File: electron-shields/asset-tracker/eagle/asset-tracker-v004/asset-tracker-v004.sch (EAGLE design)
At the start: 23 parts, among them J1 1X2-3.5MM, T1 DMG3415, U1 PAM-7Q-GPS-TH, U3 LIS3DHTR, X1 ELECTRON

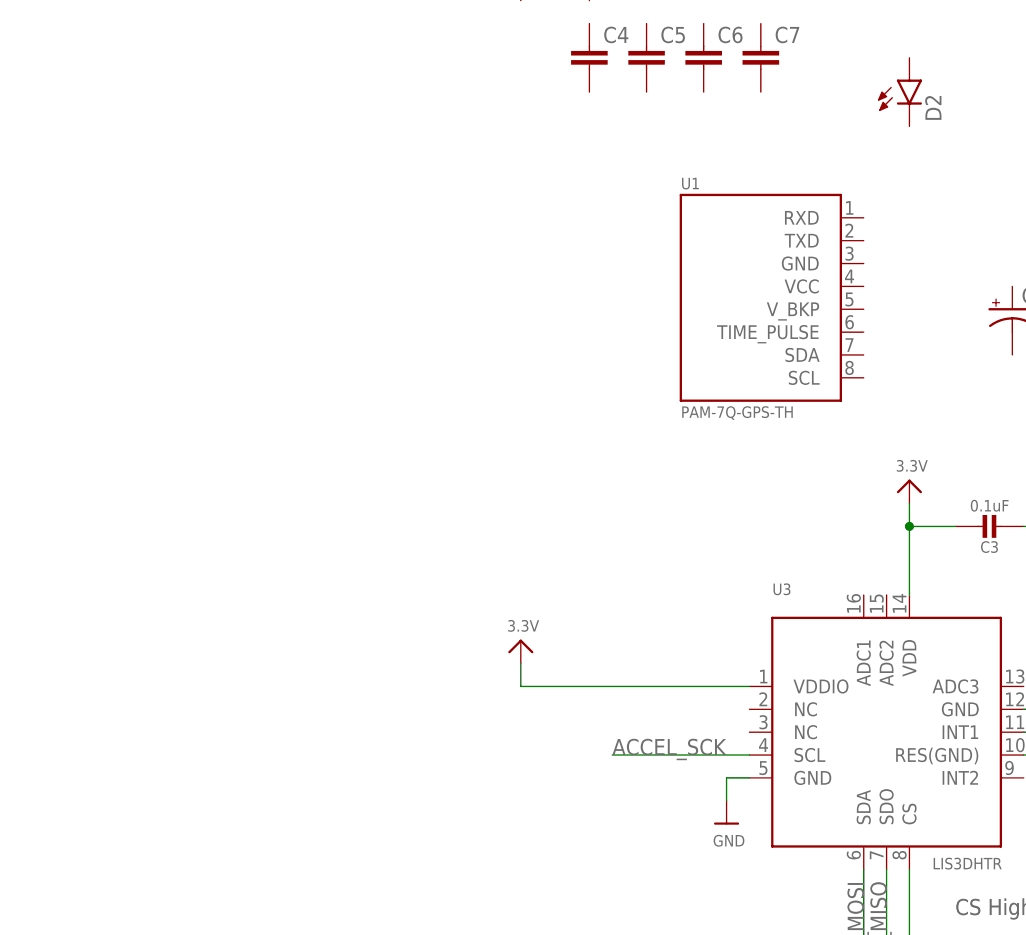
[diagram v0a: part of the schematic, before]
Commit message: added max-m8 gps and max2674 ant switch packages
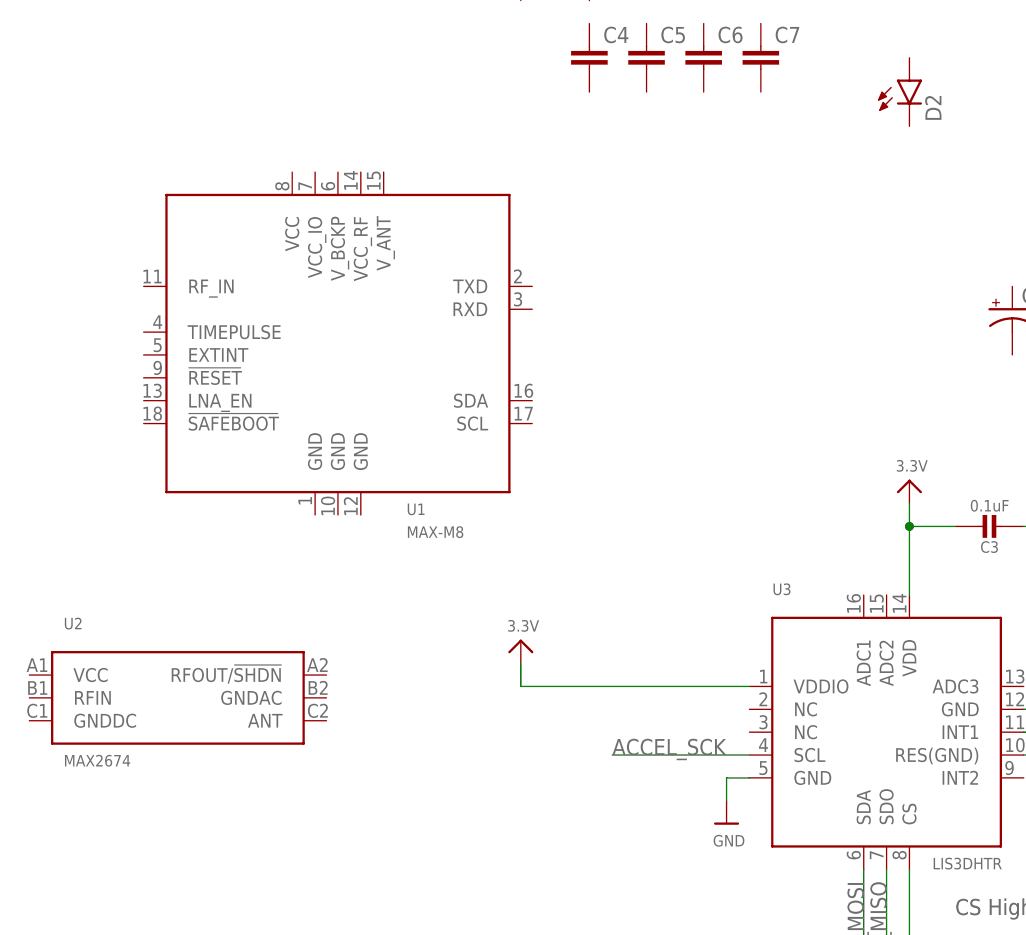
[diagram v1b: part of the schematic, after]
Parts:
- added U2: MAX2674, maxim:MAX2674
- U1: value PAM-7Q-GPS-TH -> MAX-M8; device u-blox:PAM-7Q-GPS-TH -> u-blox:MAX-M8
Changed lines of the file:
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@@
 <parts>
 <part name="FRAME1" library="frames" deviceset="LETTER_L" device=""/>
-<part name="U1" library="u-blox" deviceset="PAM-7Q-GPS" device="-TH"/>
 <part name="C1" library="adafruit" deviceset="SUPERCAP" device=""/>
 <part name="U3" library="microbuilder" deviceset="ACCEL_LIS3DHTR" device="" value="LIS3DHTR"/>
@@
 <part name="C8" library="rcl" deviceset="C-EU" device="C0603K"/>
 <part name="C9" library="rcl" deviceset="C-EU" device="C0603K"/>
+<part name="U1" library="u-blox" deviceset="MAX-M8" device=""/>
+<part name="U2" library="maxim" deviceset="MAX2674" device=""/>
 </parts>
 <sheets>
@@
 <instance part="FRAME1" gate="G$1" x="0" y="0"/>
 <instance part="FRAME1" gate="G$2" x="147.32" y="0"/>
-<instance part="U1" gate="U" x="115.57" y="130.81"/>
 <instance part="C1" gate="G$1" x="143.51" y="129.54"/>
 <instance part="U3" gate="G$1" x="129.54" y="82.55"/>
@@
 <instance part="C8" gate="G$1" x="96.52" y="168.91"/>
 <instance part="C9" gate="G$1" x="88.9" y="168.91"/>
+<instance part="U1" gate="MAX-M8" x="68.58" y="124.46"/>
+<instance part="U2" gate="MAX2674" x="50.8" y="86.36"/>
 </instances>
 <busses>

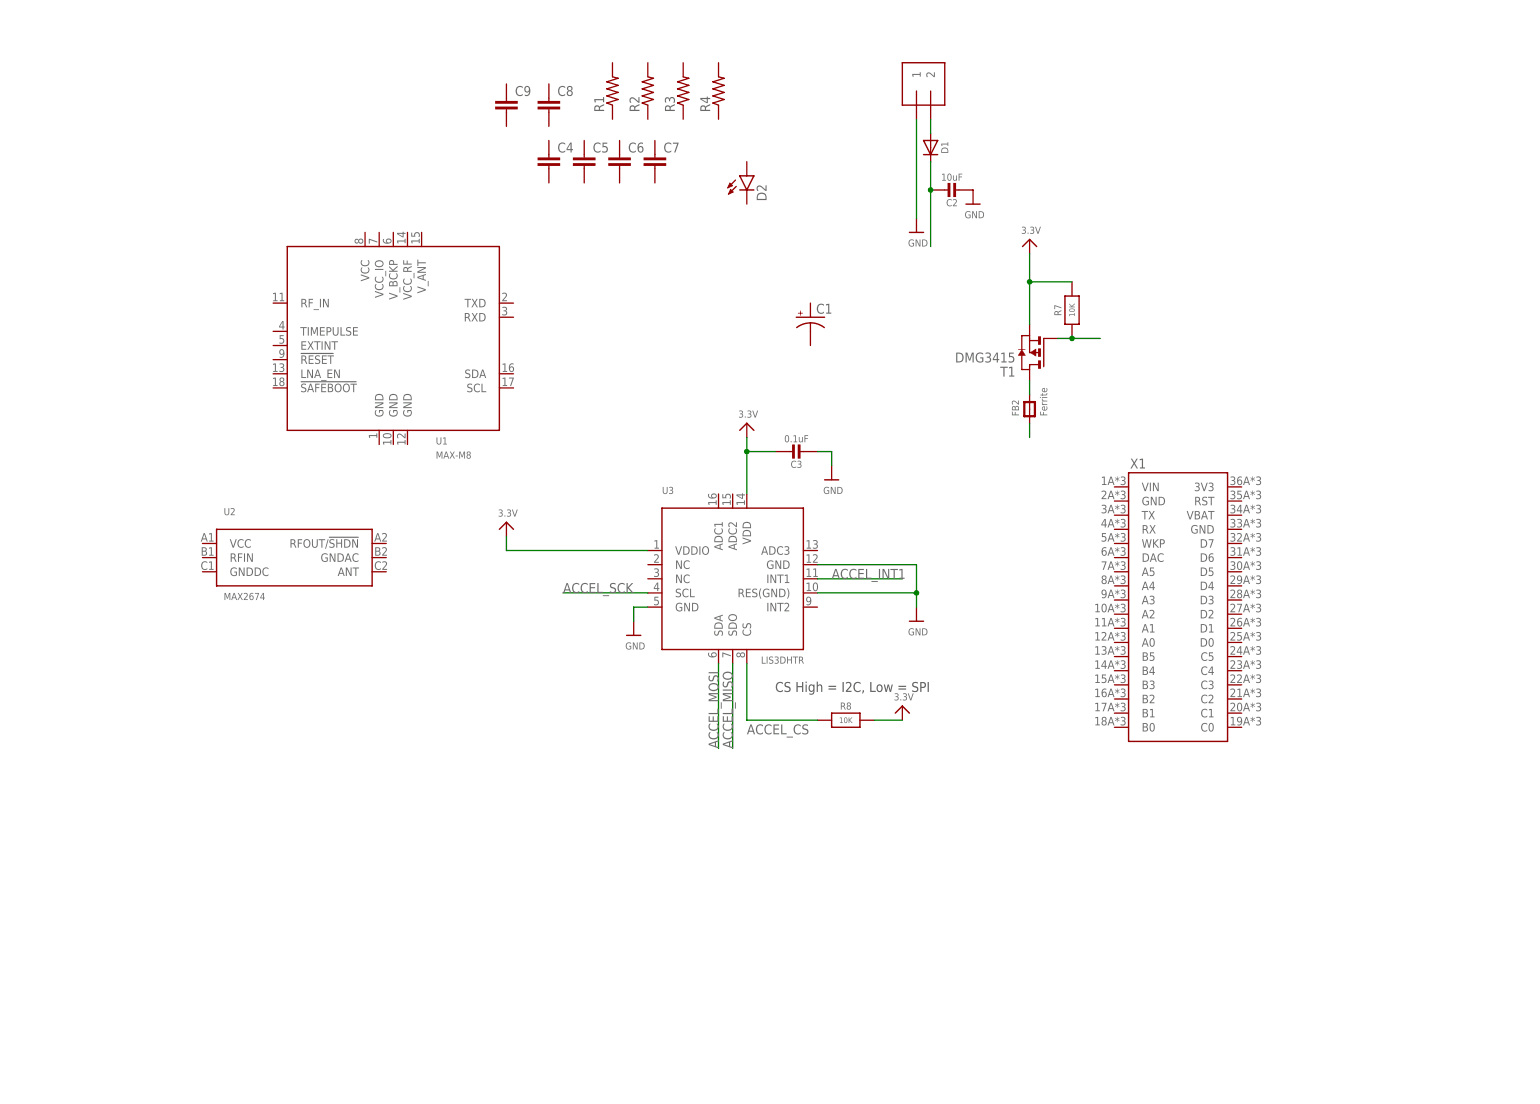
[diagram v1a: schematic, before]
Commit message: updated schematic and added more data sheets
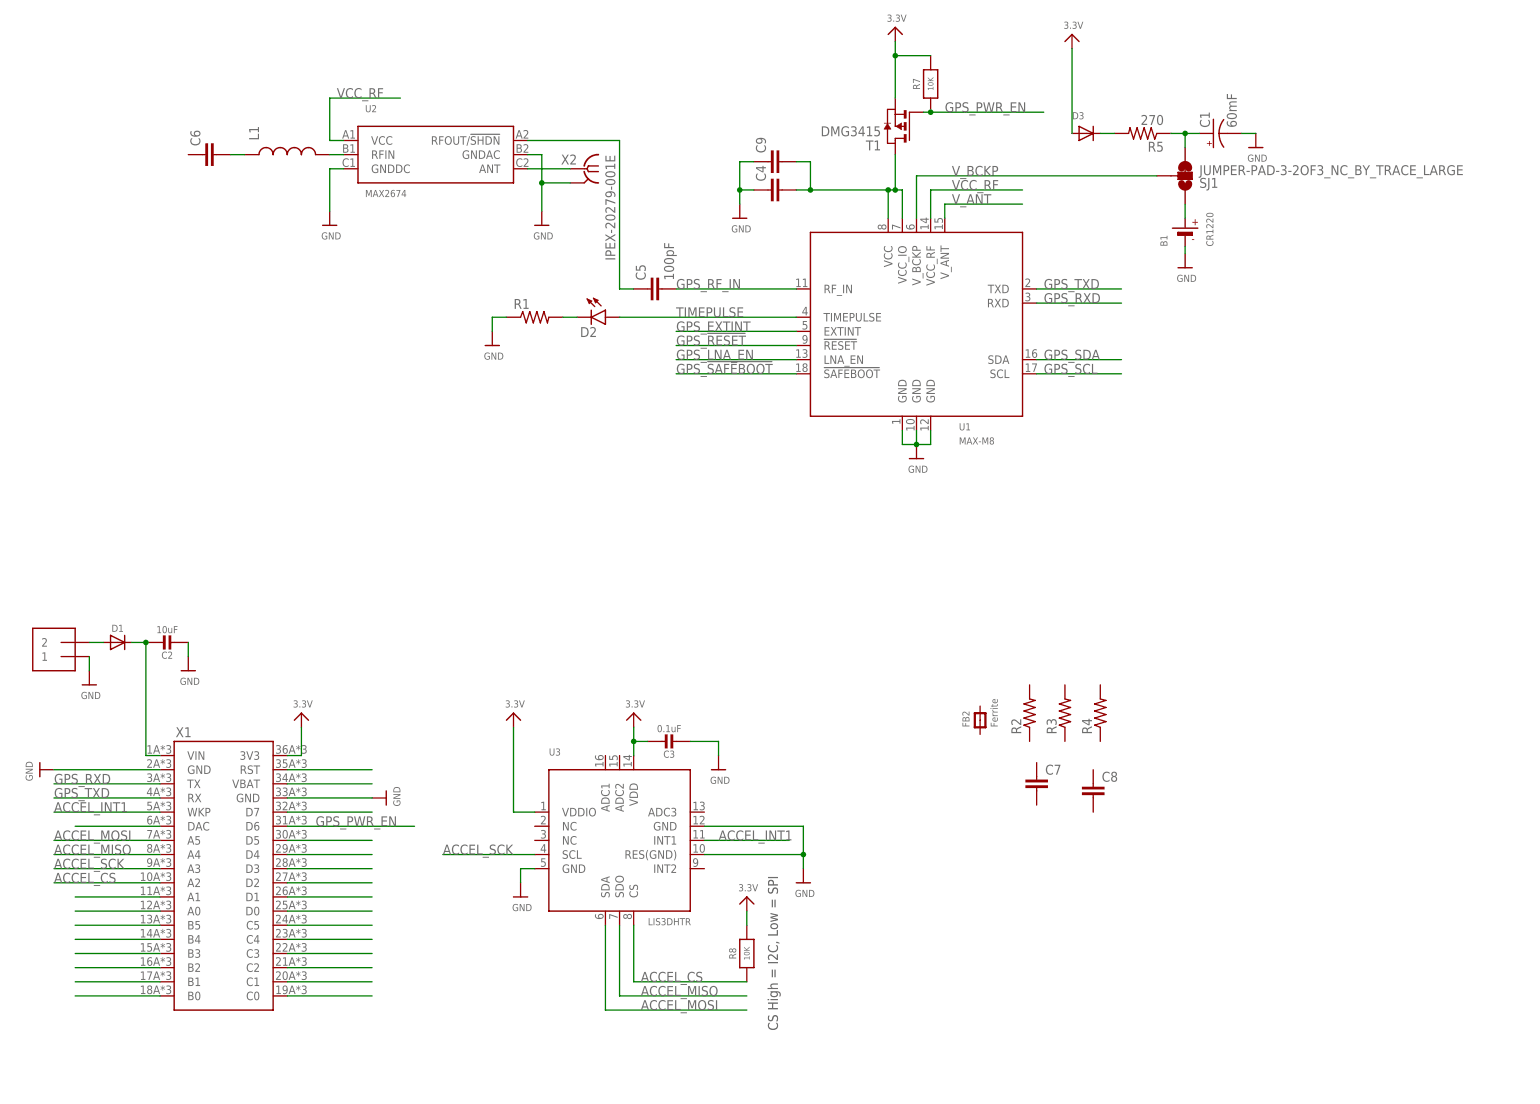
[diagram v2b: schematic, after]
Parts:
- added B1: CR1220, microbuilder:BATTERYCR1220_SMT
- added D3: (no value), adafruit:DIODESOD-523
- added L1: (no value), Particle:INDUCTOR-SPARKFUN0402
- added R5: 270, rcl:R-US_R0603
- added SJ1: JUMPER-PAD-3-2OF3_NC_BY_TRACE_LARGE, SparkFun-Passives:JUMPER-PAD-3-2OF3_NC_BY_TRACE_LARGE
- added X2: IPEX-20279-001E, Particle:IPEX-20279-001E
- C1: value (none) -> 60mF
- C5: value (none) -> 100pF
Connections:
- new net GPS_!RESET: U1.!RESET
- new net GPS_!SAFEBOOT: U1.!SAFEBOOT
- new net GPS_EXTINT: U1.EXTINT
- new net GPS_LNA_EN: U1.LNA_EN
- new net GPS_PWR_EN: R7.1, T1.G, X1.D6
- new net GPS_RF_IN: C5.2, U1.RF_IN
- new net GPS_RXD: U1.RXD, X1.TX
- new net GPS_SCL: U1.SCL
- new net GPS_SDA: U1.SDA
- new net GPS_TXD: U1.TXD, X1.RX
- new net N$10: D3.C, R5.2
- new net N$11: B1.+, SJ1.1
- new net N$4: C5.1, U2.RFOUT/!SHDN
- new net N$43: X1.DAC
- new net N$48: X1.A1
- new net N$49: X1.A0
- new net N$5: U2.ANT, X2.1
- new net N$57: X1.B5
- new net N$58: X1.B4
- new net N$59: X1.B3
- new net N$6: D2.C, R1.2
- new net N$60: X1.B2
- new net N$61: X1.B1
- new net N$62: X1.B0
- new net N$63: X1.C0
- new net N$64: X1.C1
- new net N$65: X1.C2
- new net N$66: X1.C3
- new net N$67: X1.C4
- new net N$68: X1.C5
- new net N$69: X1.D0
- new net N$7: C1.+, R5.1, SJ1.3
- new net N$70: X1.D1
- new net N$71: X1.D2
- new net N$72: X1.D3
- new net N$73: X1.D4
- new net N$74: X1.D5
- new net N$76: X1.D7
- new net N$78: X1.VBAT
- new net N$79: X1.RST
- new net TIMEPULSE: D2.A, U1.TIMEPULSE
- new net VCC_RF: U1.VCC_RF, U2.VCC
- new net V_ANT: U1.V_ANT
- new net V_BCKP: SJ1.2, U1.V_BCKP
- net 3.3V: now also D3.A, X1.3V3
- net ACCEL_CS: now also X1.A2
- net ACCEL_INT1: now also X1.WKP
- net ACCEL_MISO: now also X1.A4
- net ACCEL_MOSI: now also X1.A5
- net ACCEL_SCK: now also X1.A3
- net GND: now also B1.-, C1.-, C4.1, C9.1, R1.1, U1.GND@1, U1.GND@10, U1.GND@12, U2.GNDAC, U2.GNDDC, X1.GND, X1.GND@2, X2.GND@1
- net N$1: now also C4.2, C9.2, U1.VCC, U1.VCC_IO; no longer FB2.P$2
- net N$2: now also L1.2, U2.RFIN; no longer FB2.P$1
- net N$3: now also C6.2, L1.1; no longer R7.1, T1.G
- net N$8: now also X1.VIN
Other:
- moved on the sheet: C1, C2, C3, C4, C5, C6, C7, C8, C9, D1, D2, FB2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

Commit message: added patch antenna and enclosure outline
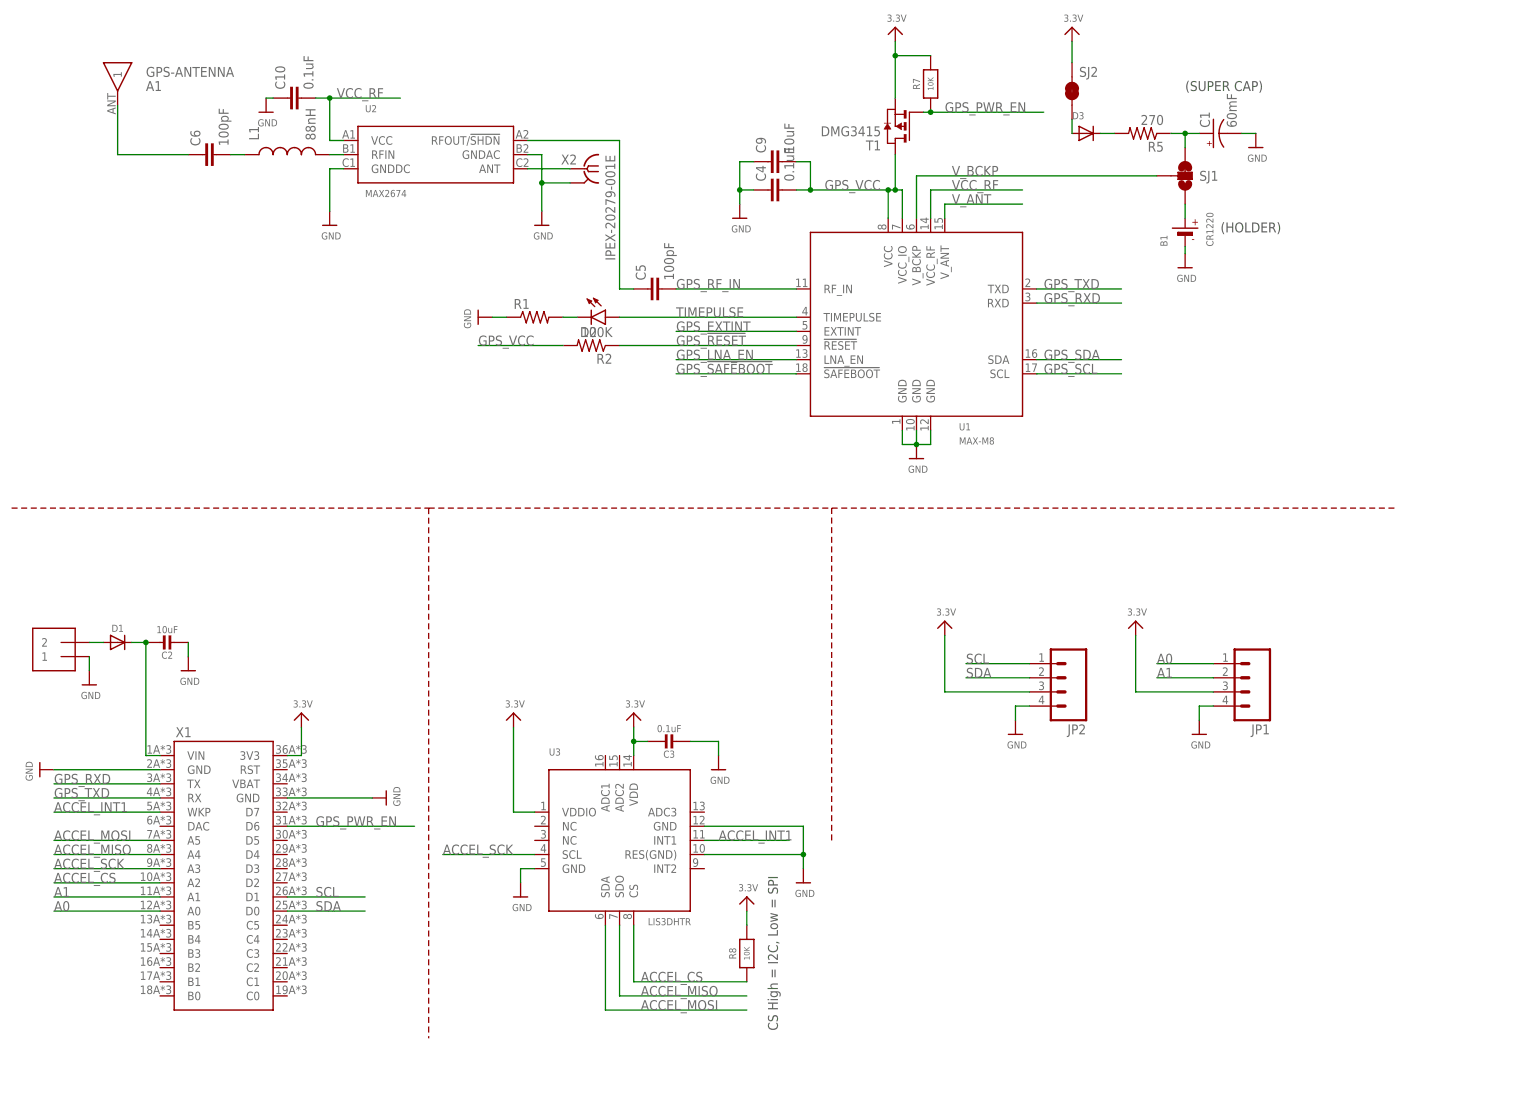
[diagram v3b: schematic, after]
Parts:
- removed C7: (no value), rcl:C-EUC0402
- removed C8: (no value), rcl:C-EUC0603K
- removed FB2: Ferrite, microbuilder:FERRITE-0805NO
- removed R3, R4: (no value), rcl:R-US_R0402
- added A1: GPS-ANTENNA, antenna:GPS-ANTENNA
- added C10: 0.1uF, rcl:C-EUC0402
- added JP1, JP2: (no value), SparkFun-Connectors:M041X04_NO_SILK
- added SJ2: JUMPER-PAD-2-NC_BY_TRACENO_SILK, SparkFun-Passives:JUMPER-PAD-2-NC_BY_TRACENO_SILK
- C4: value (none) -> 0.1uF
- C6: value (none) -> 100pF
- C9: value (none) -> 10uF
- L1: value (none) -> 88nH
- R2: value (none) -> 100K
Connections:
- removed net N$43: X1.DAC
- removed net N$48: X1.A1
- removed net N$49: X1.A0
- removed net N$57: X1.B5
- removed net N$58: X1.B4
- removed net N$59: X1.B3
- removed net N$60: X1.B2
- removed net N$61: X1.B1
- removed net N$62: X1.B0
- removed net N$63: X1.C0
- removed net N$64: X1.C1
- removed net N$65: X1.C2
- removed net N$66: X1.C3
- removed net N$67: X1.C4
- removed net N$68: X1.C5
- removed net N$69: X1.D0
- removed net N$70: X1.D1
- removed net N$71: X1.D2
- removed net N$72: X1.D3
- removed net N$73: X1.D4
- removed net N$74: X1.D5
- removed net N$76: X1.D7
- removed net N$78: X1.VBAT
- removed net N$79: X1.RST
- new net A0: JP1.1, X1.A0
- new net A1: JP1.2, X1.A1
- new net GPS_VCC: C4.2, C9.2, R2.2, T1.D, U1.VCC, U1.VCC_IO
- new net N$12: A1.1, C6.1
- new net SCL: JP2.1, X1.D1
- new net SDA: JP2.2, X1.D0
- net 3.3V: now also JP1.3, JP2.3, SJ2.2; no longer D3.A
- net GND: now also C10.1, JP1.4, JP2.4
- net GPS_!RESET: now also R2.1
- net N$1: now also D3.A, SJ2.1; no longer C4.2, C9.2, T1.D, U1.VCC, U1.VCC_IO
- net VCC_RF: now also C10.2
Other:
- note added: "(HOLDER)"
- note added: "(SUPER CAP)"
- moved on the sheet: R2
